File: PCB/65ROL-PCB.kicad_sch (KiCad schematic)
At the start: 141 parts, among them SW0 SW_Push, SW1 SW_Push, SW2 SW_Push, SW3 SW_Push, SW4 SW_Push, SW5 SW_Push, SW6 SW_Push, SW7 SW_Push, SW8 SW_Push, SW9 SW_Push

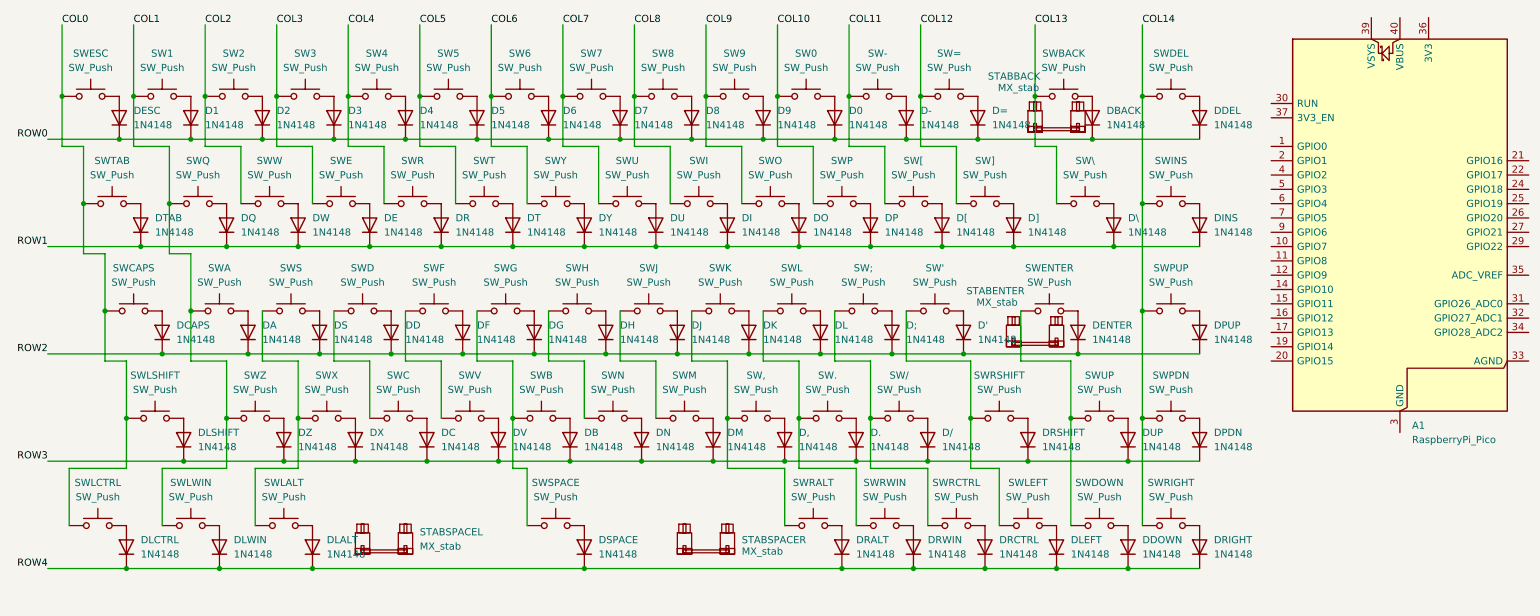
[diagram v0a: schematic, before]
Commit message: Finished basic key schematic and linked footprints
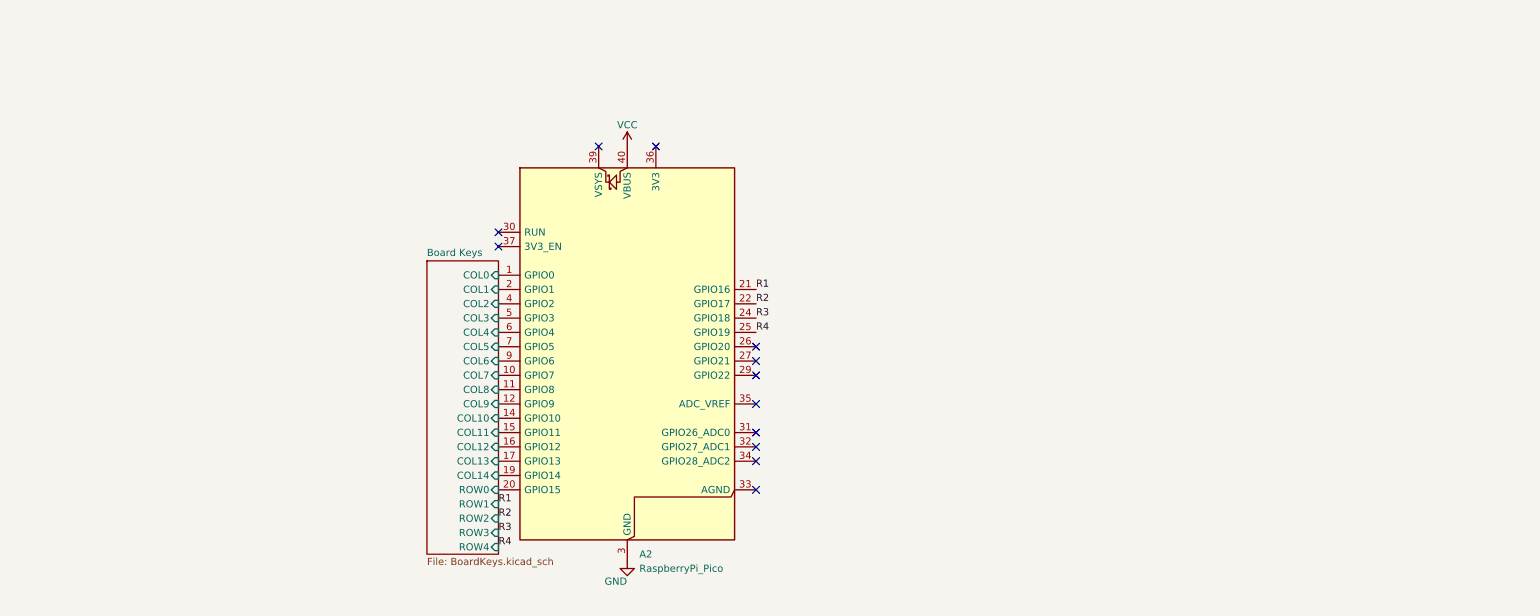
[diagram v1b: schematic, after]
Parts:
- removed A1: RaspberryPi_Pico, Module:RaspberryPi_Pico_Common_Unspecified, symbol MCU_Module:RaspberryPi_Pico
- removed D', D,, D-, D., D/, D0, D1, D2, D3, D4, D5, D6, D7, D8, D9, D;, D=, DA, DB, DBACK, DC, DCAPS, DD, DDEL, DDOWN, DE, DENTER, DESC, DF, DG, DH, DI, DINS, DJ, DK, DL, DLALT, DLCTRL, DLEFT, DLSHIFT, DLWIN, DM, DN, DO, DP, DPDN, DPUP, DQ, DR, DRALT, DRCTRL, DRIGHT, DRSHIFT, DRWIN, DS, DSPACE, DT, DTAB, DU, DUP, DV, DW, DX, DY, DZ, D[, D\, D]: 1N4148, Diode_THT:D_DO-35_SOD27_P7.62mm_Horizontal, symbol Diode:1N4148
- removed STABBACK, STABENTER, STABSPACEL, STABSPACER: MX_stab, PCM_marbastlib-mx:STAB_MX_P_6.25u, symbol PCM_marbastlib-mx:MX_stab
- removed SW', SW,, SW-, SW., SW/, SW0, SW1, SW2, SW3, SW4, SW5, SW6, SW7, SW8, SW9, SW;, SW=, SWA, SWB, SWBACK, SWC, SWCAPS, SWD, SWDEL, SWDOWN, SWE, SWENTER, SWESC, SWF, SWG, SWH, SWI, SWINS, SWJ, SWK, SWL, SWLALT, SWLCTRL, SWLEFT, SWLSHIFT, SWLWIN, SWM, SWN, SWO, SWP, SWPDN, SWPUP, SWQ, SWR, SWRALT, SWRCTRL, SWRIGHT, SWRSHIFT, SWRWIN, SWS, SWSPACE, SWT, SWTAB, SWU, SWUP, SWV, SWW, SWX, SWY, SWZ, SW[, SW\, SW]: SW_Push, symbol Switch:SW_Push
- added A2: RaspberryPi_Pico, Module:RaspberryPi_Pico_Common_THT, symbol MCU_Module:RaspberryPi_Pico
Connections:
- new net Board Keys/COL0: A2.1 (GPIO0)
- new net Board Keys/COL1: A2.2 (GPIO1)
- new net Board Keys/COL10: A2.14 (GPIO10)
- new net Board Keys/COL11: A2.15 (GPIO11)
- new net Board Keys/COL12: A2.16 (GPIO12)
- new net Board Keys/COL13: A2.17 (GPIO13)
- new net Board Keys/COL14: A2.19 (GPIO14)
- new net Board Keys/COL2: A2.4 (GPIO2)
- new net Board Keys/COL3: A2.5 (GPIO3)
- new net Board Keys/COL4: A2.6 (GPIO4)
- new net Board Keys/COL5: A2.7 (GPIO5)
- new net Board Keys/COL6: A2.9 (GPIO6)
- new net Board Keys/COL7: A2.10 (GPIO7)
- new net Board Keys/COL8: A2.11 (GPIO8)
- new net Board Keys/COL9: A2.12 (GPIO9)
- new net Board Keys/ROW0: A2.20 (GPIO15)
- new net GND: A2.13 (GND), A2.18 (GND), A2.23 (GND), A2.28 (GND), A2.3 (GND), A2.38 (GND), A2.8 (GND)
- new net R1: A2.21 (GPIO16)
- new net R2: A2.22 (GPIO17)
- new net R3: A2.24 (GPIO18)
- new net R4: A2.25 (GPIO19)
- new net VCC: A2.40 (VBUS)
- no-connect marks 0 -> 12
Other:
- added sheet Board Keys (BoardKeys.kicad_sch)
- company: (none) -> Liam Ramirez-Guess
- title: (none) -> BigSaltyKeyboard-65ROL

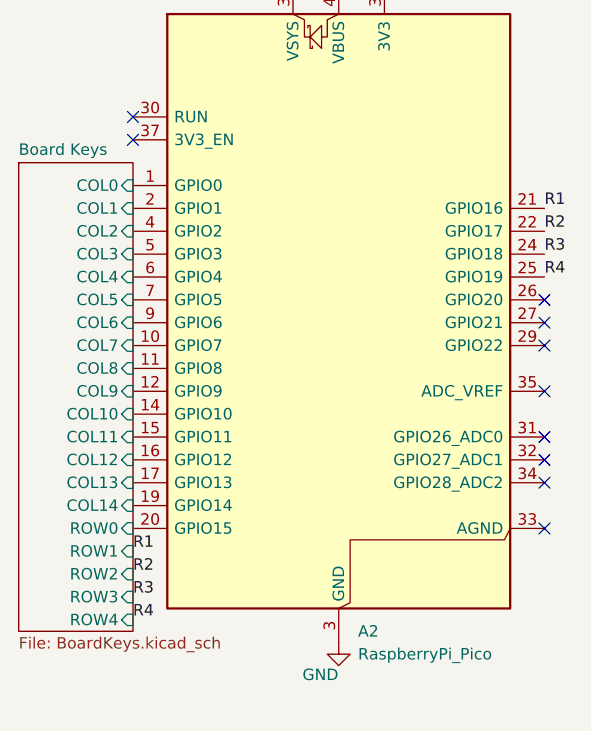
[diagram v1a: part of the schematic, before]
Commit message: Placed all diodes and made edge
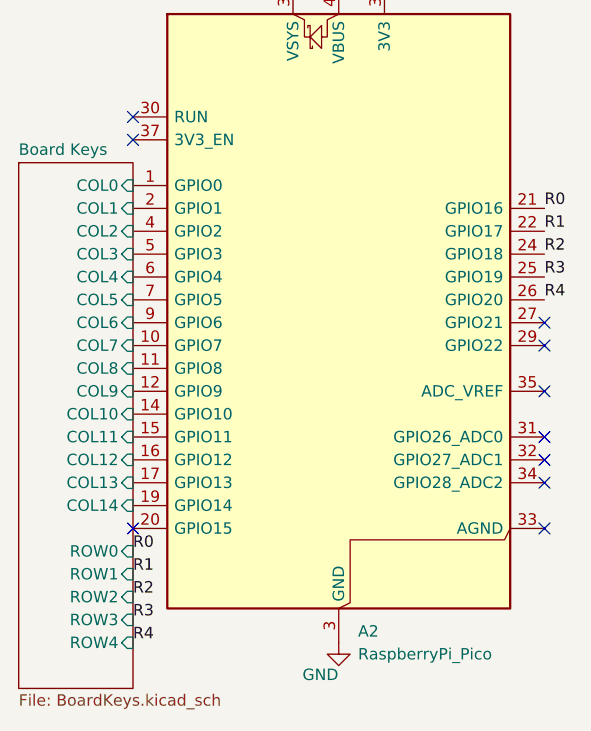
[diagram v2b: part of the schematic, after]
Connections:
- net R1: now also A2.22 (GPIO17); no longer A2.21 (GPIO16)
- net R2: now also A2.24 (GPIO18); no longer A2.22 (GPIO17)
- net R3: now also A2.25 (GPIO19); no longer A2.24 (GPIO18)
- net R4: now also A2.26 (GPIO20); no longer A2.25 (GPIO19)
- net Board Keys/ROW0: no longer names the net of A2.20 (GPIO15)
- new net R0: A2.21 (GPIO16)
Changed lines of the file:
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@@
-	)
-	(no_connect
-		(at 148.59 74.93)
 	)
 	(no_connect
@@
 	)
 	(no_connect
+		(at 102.87 100.33)
+	)
+	(no_connect
 		(at 102.87 54.61)
 	)
@@
 	)
 	(label "R4"
+		(at 102.87 113.03 0)
+		(effects
+			(font
+				(size 1.27 1.27)
+			)
+			(justify left bottom)
+		)
+	)
+	(label "R3"
 		(at 102.87 110.49 0)
 		(effects
@@
 		)
 	)
+	(label "R0"
+		(at 148.59 64.77 0)
+		(effects
+			(font
+				(size 1.27 1.27)
+			)
+			(justify left bottom)
+		)
+	)
+	(label "R4"
+		(at 148.59 74.93 0)
+		(effects
+			(font
+				(size 1.27 1.27)
+			)
+			(justify left bottom)
+		)
+	)
+	(label "R1"
+		(at 148.59 67.31 0)
+		(effects
+			(font
+				(size 1.27 1.27)
+			)
+			(justify left bottom)
+		)
+	)
+	(label "R0"
+		(at 102.87 102.87 0)
+		(effects
+			(font
+				(size 1.27 1.27)
+			)
+			(justify left bottom)
+		)
+	)
+	(label "R2"
+		(at 148.59 69.85 0)
+		(effects
+			(font
+				(size 1.27 1.27)
+			)
+			(justify left bottom)
+		)
+	)
+	(label "R1"
+		(at 102.87 105.41 0)
+		(effects
+			(font
+				(size 1.27 1.27)
+			)
+			(justify left bottom)
+		)
+	)
+	(label "R2"
+		(at 102.87 107.95 0)
+		(effects
+			(font
+				(size 1.27 1.27)
+			)
+			(justify left bottom)
+		)
+	)
 	(label "R3"
-		(at 102.87 107.95 0)
-		(effects
-			(font
-				(size 1.27 1.27)
-			)
-			(justify left bottom)
-		)
-	)
-	(label "R4"
 		(at 148.59 72.39 0)
-		(effects
-			(font
-				(size 1.27 1.27)
-			)
-			(justify left bottom)
-		)
-	)
-	(label "R1"
-		(at 148.59 64.77 0)
-		(effects
-			(font
-				(size 1.27 1.27)
-			)
-			(justify left bottom)
-		)
-	)
-	(label "R2"
-		(at 148.59 67.31 0)
-		(effects
-			(font
-				(size 1.27 1.27)
-			)
-			(justify left bottom)
-		)
-	)
-	(label "R1"
-		(at 102.87 102.87 0)
-		(effects
-			(font
-				(size 1.27 1.27)
-			)
-			(justify left bottom)
-		)
-	)
-	(label "R2"
-		(at 102.87 105.41 0)
-		(effects
-			(font
-				(size 1.27 1.27)
-			)
-			(justify left bottom)
-		)
-	)
-	(label "R3"
-		(at 148.59 69.85 0)
 		(effects
 			(font
@@
 	(sheet
 		(at 90.17 59.69)
-		(size 12.7 52.07)
+		(size 12.7 58.42)
 		(exclude_from_sim no)
 		(in_bom yes)
@@
 		)
 		(property "Sheetfile" "BoardKeys.kicad_sch"
-			(at 90.17 112.3446 0)
+			(at 90.17 118.6946 0)
 			(show_name no)
 			(do_not_autoplace no)
@@
 		)
 		(pin "ROW0" input
-			(at 102.87 100.33 0)
+			(at 102.87 102.87 0)
 			(effects
 				(font
@@
 		)
 		(pin "ROW1" input
-			(at 102.87 102.87 0)
+			(at 102.87 105.41 0)
 			(effects
 				(font
@@
 		)
 		(pin "ROW2" input
-			(at 102.87 105.41 0)
+			(at 102.87 107.95 0)
 			(effects
 				(font
@@
 		)
 		(pin "ROW3" input
-			(at 102.87 107.95 0)
+			(at 102.87 110.49 0)
 			(effects
 				(font
@@
 		)
 		(pin "ROW4" input
-			(at 102.87 110.49 0)
-			(effects
-				(font
+			(at 102.87 113.03 0)
+			(effects
+				(font

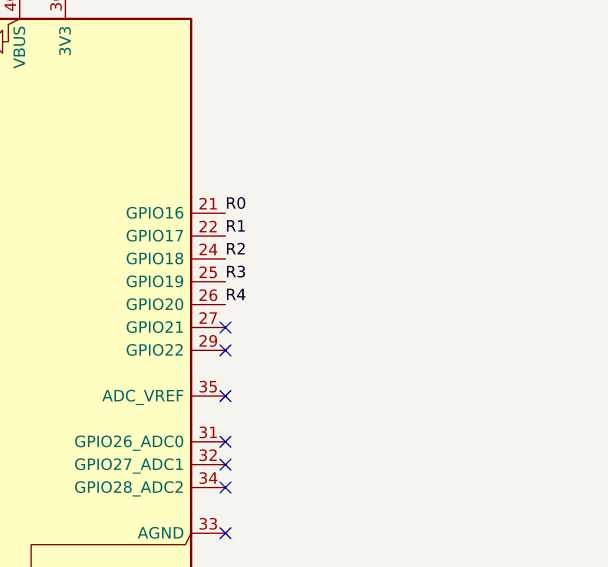
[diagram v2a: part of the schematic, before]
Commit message: Added LEDs to schematic and PCB
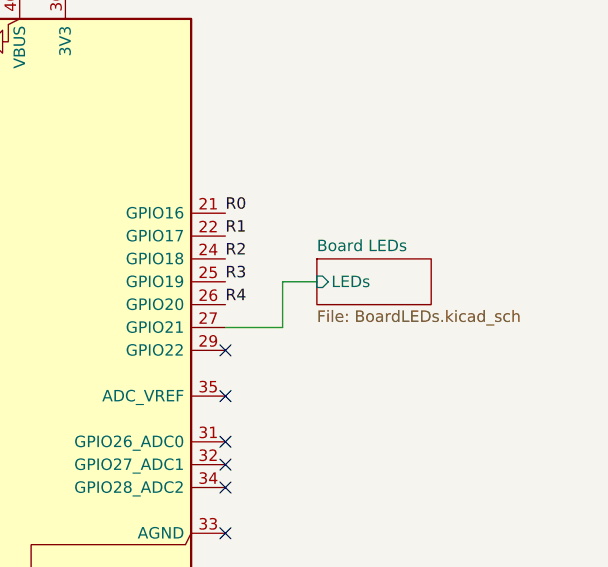
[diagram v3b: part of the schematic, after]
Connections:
- net Board LEDs/LEDs: now reaches A2.27 (GPIO21)
- no-connect marks 12 -> 11
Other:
- added sheet Board LEDs (BoardLEDs.kicad_sch)
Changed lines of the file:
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@@
-	)
-	(no_connect
-		(at 148.59 77.47)
 	)
 	(no_connect
@@
 	(no_connect
 		(at 130.81 39.37)
+	)
+	(wire
+		(pts
+			(xy 154.94 77.47) (xy 154.94 72.39)
+		)
+		(stroke
+			(width 0)
+			(type default)
+		)
+	)
+	(wire
+		(pts
+			(xy 154.94 72.39) (xy 158.75 72.39)
+		)
+		(stroke
+			(width 0)
+			(type default)
+		)
+	)
+	(wire
+		(pts
+			(xy 148.59 77.47) (xy 154.94 77.47)
+		)
+		(stroke
+			(width 0)
+			(type default)
+		)
 	)
 	(label "R4"
@@
 				)
 			)
+		)
+	)
+	(sheet
+		(at 158.75 69.85)
+		(size 12.7 5.08)
+		(exclude_from_sim no)
+		(in_bom yes)
+		(on_board yes)
+		(dnp no)
+		(fields_autoplaced yes)
+		(stroke
+			(width 0.1524)
+			(type solid)
+		)
+		(fill
+			(color 0 0 0 0)
+		)
+		(property "Sheetname" "Board LEDs"
+			(at 158.75 69.1384 0)
+			(show_name no)
+			(do_not_autoplace no)
+			(effects
+				(font
+					(size 1.27 1.27)
+				)
+				(justify left bottom)
+			)
+		)
+		(property "Sheetfile" "BoardLEDs.kicad_sch"
+			(at 158.75 75.5146 0)
+			(show_name no)
+			(do_not_autoplace no)
+			(effects
+				(font
+					(size 1.27 1.27)
+				)
+				(justify left top)
+			)
+		)
+		(pin "LEDs" input
+			(at 158.75 72.39 180)
+			(effects
+				(font
+					(size 1.27 1.27)
+				)
+				(justify left)
+			)
+		)
+		(instances
+			(project "65ROL-PCB"
+				(path "/346f8378-20cc-482f-b93f-6d5e3bddbc25"
+					(page "3")
+				)
+			)

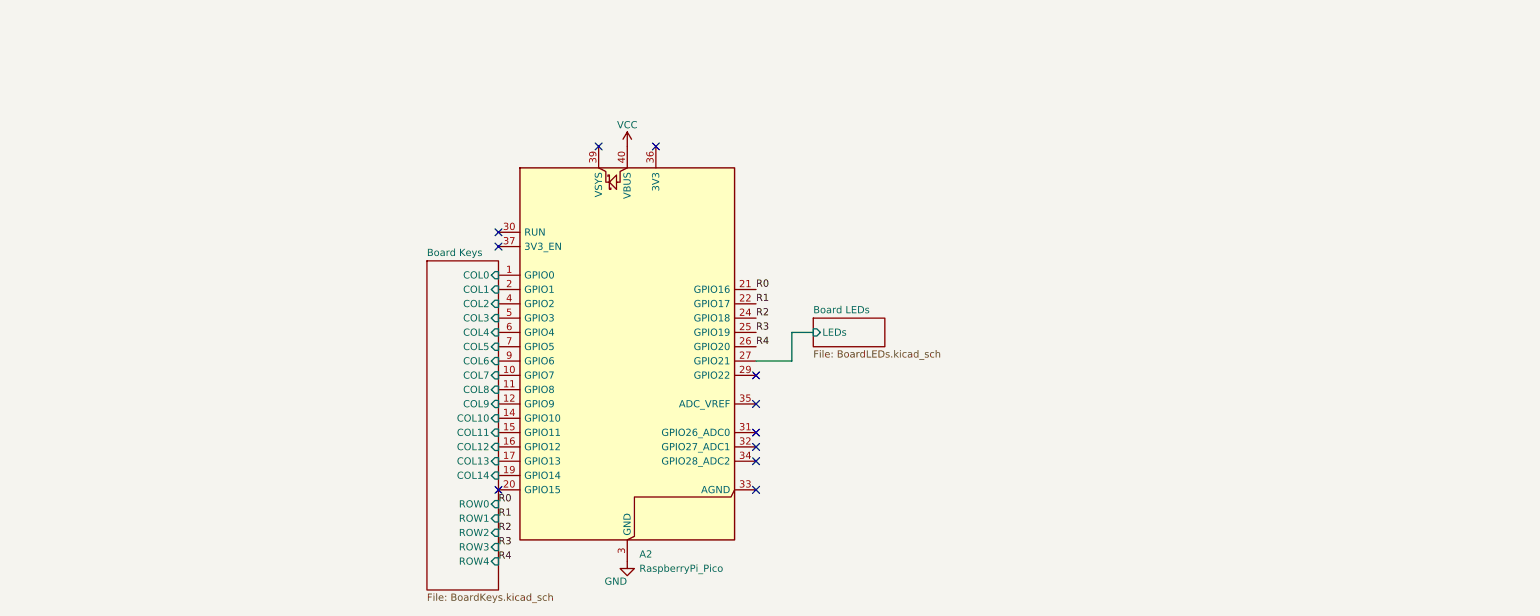
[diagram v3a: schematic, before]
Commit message: Added Scematic for rear extention and LED logic shifter, decoupling capacitors and data line resitors
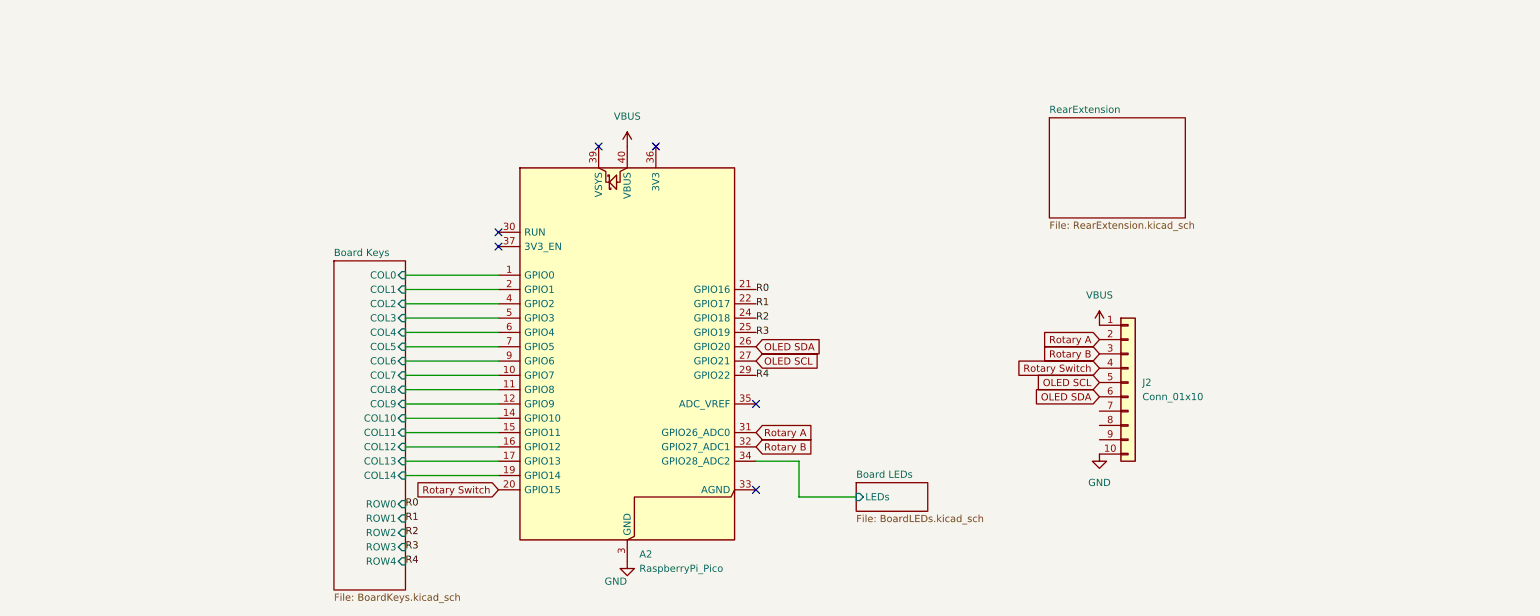
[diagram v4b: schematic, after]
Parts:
- added J2: Conn_01x10, Connector_PinHeader_1.00mm:PinHeader_1x10_P1.00mm_Horizontal, symbol Connector_Generic:Conn_01x10
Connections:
- net Board LEDs/LEDs: now also A2.34 (GPIO28_ADC2); no longer A2.27 (GPIO21)
- net GND: now also J2.10 (Pin_10)
- net R4: now also A2.29 (GPIO22); no longer A2.26 (GPIO20)
- net Rotary Switch: now reaches A2.20 (GPIO15)
- net Rotary Switch: now also J2.4 (Pin_4)
- net Rotary A: now reaches A2.31 (GPIO26_ADC0)
- net Rotary A: now also J2.2 (Pin_2)
- net Rotary B: now reaches A2.32 (GPIO27_ADC1)
- net Rotary B: now also J2.3 (Pin_3)
- net VCC renamed VBUS
- net VBUS: now also J2.1 (Pin_1)
- new net OLED SCL: A2.27 (GPIO21), J2.5 (Pin_5)
- new net OLED SDA: A2.26 (GPIO20), J2.6 (Pin_6)
- no-connect marks 11 -> 6
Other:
- added sheet RearExtension (RearExtension.kicad_sch)
